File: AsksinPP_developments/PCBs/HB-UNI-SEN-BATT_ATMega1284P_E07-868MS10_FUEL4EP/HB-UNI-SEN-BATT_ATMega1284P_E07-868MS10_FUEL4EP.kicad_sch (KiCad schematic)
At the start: 57 parts, among them J1 Conn_01x02, J10 charge, J11 ePaper connector, J12 FTDI Debuger, J2 Conn_01x02, J3 Conn_01x02, J4 Conn_01x02, J5 ISP Programmer, J6 Conn_01x04, J7 Conn_01x04, J8 Conn_01x04, J9 Conn_01x04, Q1 IRLU024N, SW1 Config button, SW2 Reset button, U1 ATmega1284P-AU, U2 TPS61221DCK, Y1 8MHz

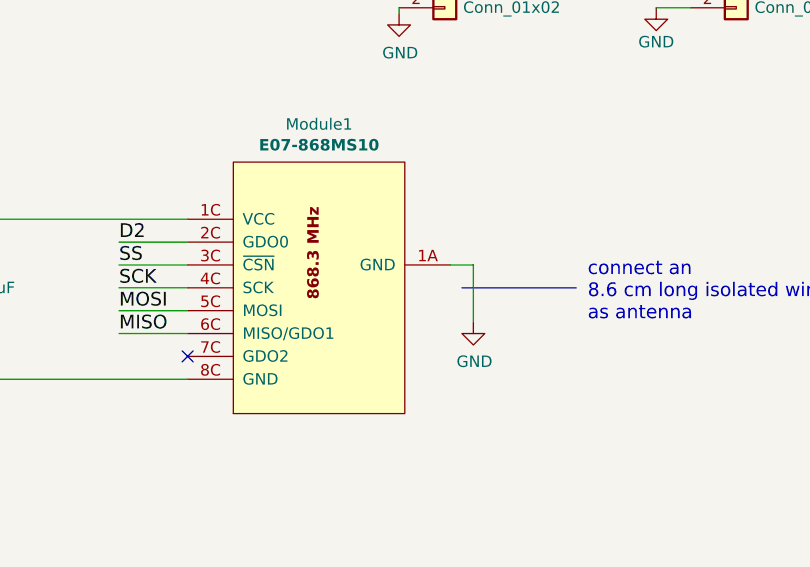
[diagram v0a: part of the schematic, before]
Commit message: PCBs: KiCAD6 required improvements of layout data bases; added E07-900M10S into FUEL and footprint library
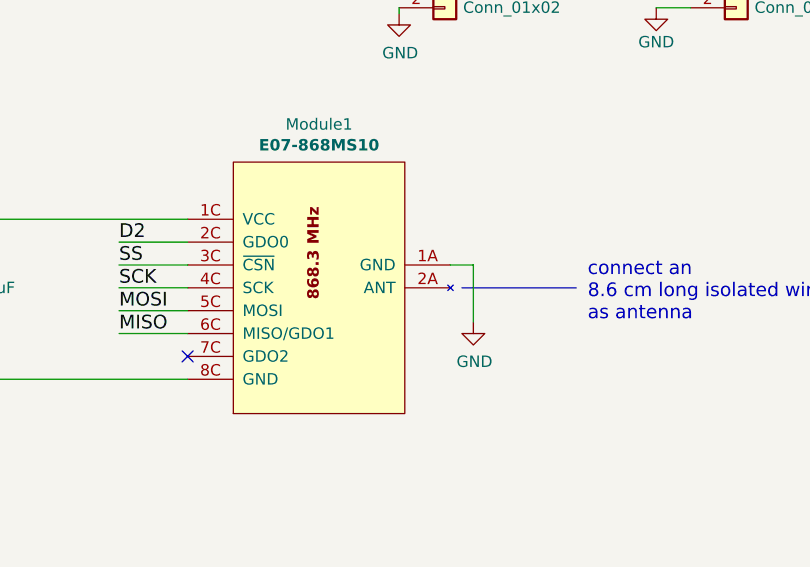
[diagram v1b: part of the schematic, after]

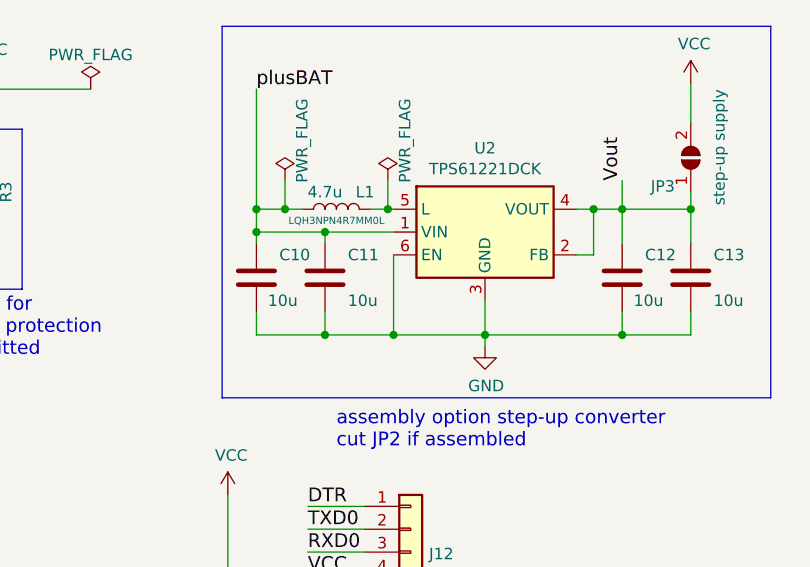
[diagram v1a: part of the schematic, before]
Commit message: HB-UNI-SEN-BATT_ATMega1284P_E07-868MS10_FUEL4EP and HB-UNI-SEN-BATT_ATMega1284P_E07-868MS10_FRAM_FUEL4EP: Fix of wrong connection of EN pin of TPS61221 boost converter
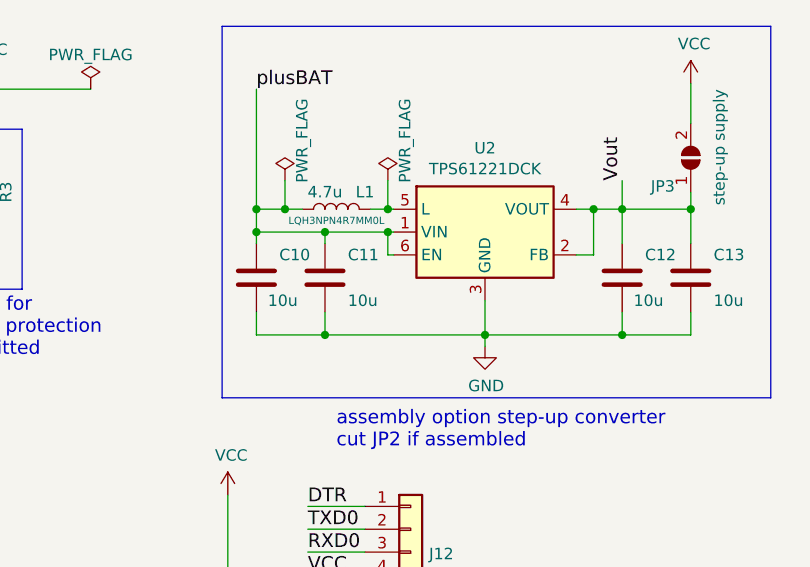
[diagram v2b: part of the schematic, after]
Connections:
- net GND: no longer U2.6 (EN)
- net plusBAT: now also U2.6 (EN)
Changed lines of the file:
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@@
   (title_block
     (title "HB-UNI-SEN-BATT_ATMega1284P_FUEL4EP")
-    (date "2023-07-16")
-    (rev "1.2")
+    (date "2023-08-15")
+    (rev "1.3")
     (company "FUEL4EP")
     (comment 1 "Creative Commons License, non-commercial")
@@
   (junction (at 55.245 28.575) (diameter 0) (color 0 0 0 0)
   )
-  (junction (at 142.24 49.53) (diameter 0) (color 0 0 0 0)
+  (junction (at 141.605 38.1) (diameter 0) (color 0 0 0 0)
   )
   (junction (at 238.76 35.56) (diameter 0) (color 0 0 0 0)
@@
     (stroke (width 0) (type default) (color 0 0 0 0))
   )
-  (wire (pts (xy 134.62 49.53) (xy 142.24 49.53))
+  (wire (pts (xy 134.62 49.53) (xy 152.4 49.53))
     (stroke (width 0) (type default) (color 0 0 0 0))
   )
@@
     (stroke (width 0) (type default) (color 0 0 0 0))
   )
+  (wire (pts (xy 141.605 38.1) (xy 134.62 38.1))
+    (stroke (width 0) (type default) (color 0 0 0 0))
+  )
   (wire (pts (xy 152.4 49.53) (xy 167.64 49.53))
     (stroke (width 0) (type default) (color 0 0 0 0))
@@
     (stroke (width 0) (type default) (color 0 0 0 0))
   )
+  (wire (pts (xy 142.24 40.64) (xy 141.605 40.64))
+    (stroke (width 0) (type default) (color 0 0 0 0))
+  )
   (wire (pts (xy 85.09 110.49) (xy 91.44 110.49))
     (stroke (width 0) (type default) (color 0 0 0 0))
@@
     (stroke (width 0) (type default) (color 0 0 0 0))
   )
+  (wire (pts (xy 141.605 40.64) (xy 141.605 38.1))
+    (stroke (width 0) (type default) (color 0 0 0 0))
+  )
   (wire (pts (xy 201.295 70.485) (xy 202.565 70.485))
     (stroke (width 0) (type default) (color 0 0 0 0))
@@
     (stroke (width 0) (type default) (color 0 0 0 0))
   )
-  (wire (pts (xy 142.24 49.53) (xy 152.4 49.53))
-    (stroke (width 0) (type default) (color 0 0 0 0))
-  )
   (wire (pts (xy 123.825 78.74) (xy 139.065 78.74))
     (stroke (width 0) (type default) (color 0 0 0 0))
@@
     (stroke (width 0) (type default) (color 0 0 0 0))
   )
-  (wire (pts (xy 142.24 40.64) (xy 142.24 49.53))
-    (stroke (width 0) (type default) (color 0 0 0 0))
-  )
   (wire (pts (xy 177.8 116.84) (xy 177.8 116.205))
     (stroke (width 0) (type default) (color 0 0 0 0))
@@
     (stroke (width 0) (type default) (color 0 0 0 0))
   )
-  (wire (pts (xy 142.24 38.1) (xy 134.62 38.1))
-    (stroke (width 0) (type default) (color 0 0 0 0))
-  )
+  (wire (pts (xy 142.24 38.1) (xy 141.605 38.1))
+    (stroke (width 0) (type default) (color 0 0 0 0))
+  )

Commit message: PCBs: added HB-UNI-SEN-BATT_ATMega1284P_E07-900MM10S_FUEL4EP; fies fixes for HB-UNI-SEN-BATT_ATMega1284P_E07-868MS10_FUEL4EP and HB-UNI-SEN-BATT_E07-900MM10S_FUEL4EP
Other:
- title: HB-UNI-SEN-BATT_ATMega1284P_FUEL4EP -> HB-UNI-SEN-BATT_ATMega1284P_E07-868MS10_FUEL4EP
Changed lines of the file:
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@@
   (paper "A4")
   (title_block
-    (title "HB-UNI-SEN-BATT_ATMega1284P_FUEL4EP")
+    (title "HB-UNI-SEN-BATT_ATMega1284P_E07-868MS10_FUEL4EP")
     (date "2023-08-15")
     (rev "1.3")

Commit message: PCBs: documentation updates / PCBs: HB-UNI-SEN-BATT_ATMega1284P_E07-868MS10_FUEL4EP, HB-UNI-SEN-BATT_ATMega1284P_E07-868MS10_FRAM_FUEL4EP, HB-UNI-SEN-BATT_ATMega1284P_E07-900MM10S_FUEL4EP: fix of wrong LCSC number for R7
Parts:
- R7: LCSC C25271 -> C149504
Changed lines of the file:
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@@
   (title_block
     (title "HB-UNI-SEN-BATT_ATMega1284P_E07-868MS10_FUEL4EP")
-    (date "2023-08-15")
-    (rev "1.3")
+    (date "2024-02-17")
+    (rev "1.4")
     (company "FUEL4EP")
     (comment 1 "Creative Commons License, non-commercial")
@@
       (effects (font (size 1.27 1.27)) hide)
     )
-    (property "Datasheet" "https://datasheet.lcsc.com/lcsc/1809140123_UNI-ROYAL-Uniroyal-Elec-0805W8F100KT5E_C25271.pdf" (id 3) (at 197.485 70.485 0)
+    (property "Datasheet" "https://datasheet.lcsc.com/lcsc/2205312316_UNI-ROYAL-Uniroyal-Elec-0805W8F1003T5E_C149504.pdf" (id 3) (at 197.485 70.485 0)
       (effects (font (size 1.27 1.27)) hide)
     )
@@
       (effects (font (size 1.27 1.27)) hide)
     )
-    (property "LCSC" "C25271" (id 5) (at 197.485 70.485 0)
-      (effects (font (size 1.27 1.27)) hide)
-    )
+    (property "LCSC" "C149504" (id 5) (at 197.485 70.485 0)
+      (effects (font (size 1.27 1.27)) hide)
+    )

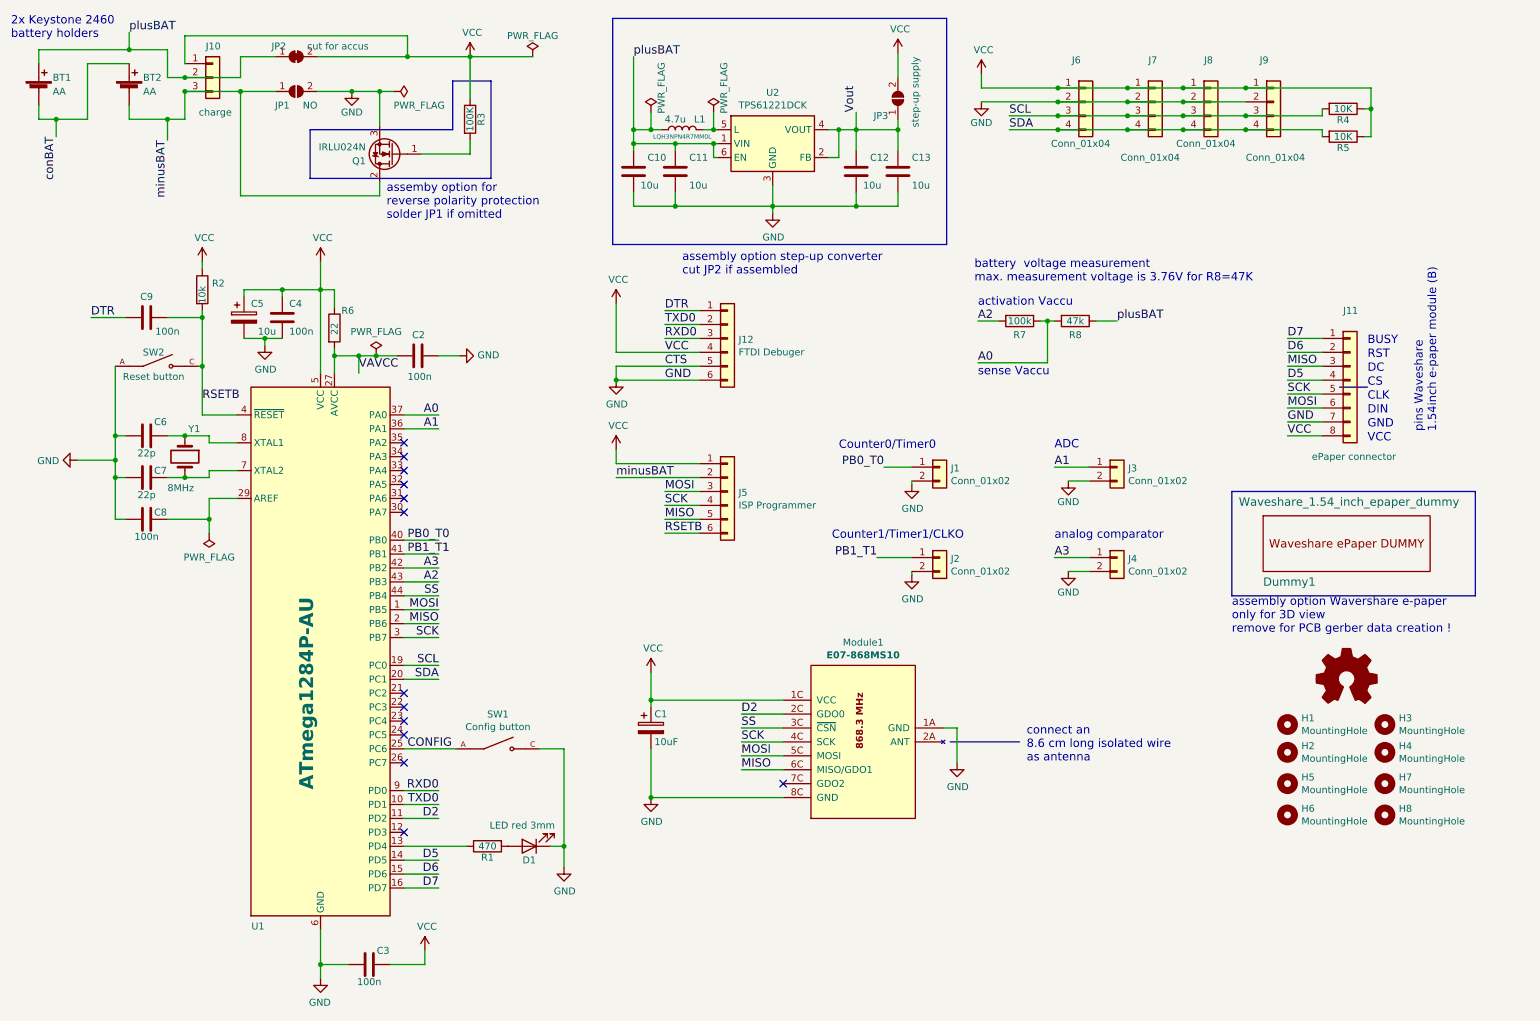
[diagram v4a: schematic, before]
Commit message: PCBs/HB-UNI-SEN-BATT_ATMega1284P_E07-868MS10_FUEL4EP: migration to KiCAD 8, x-check and fix of LCSC numbers
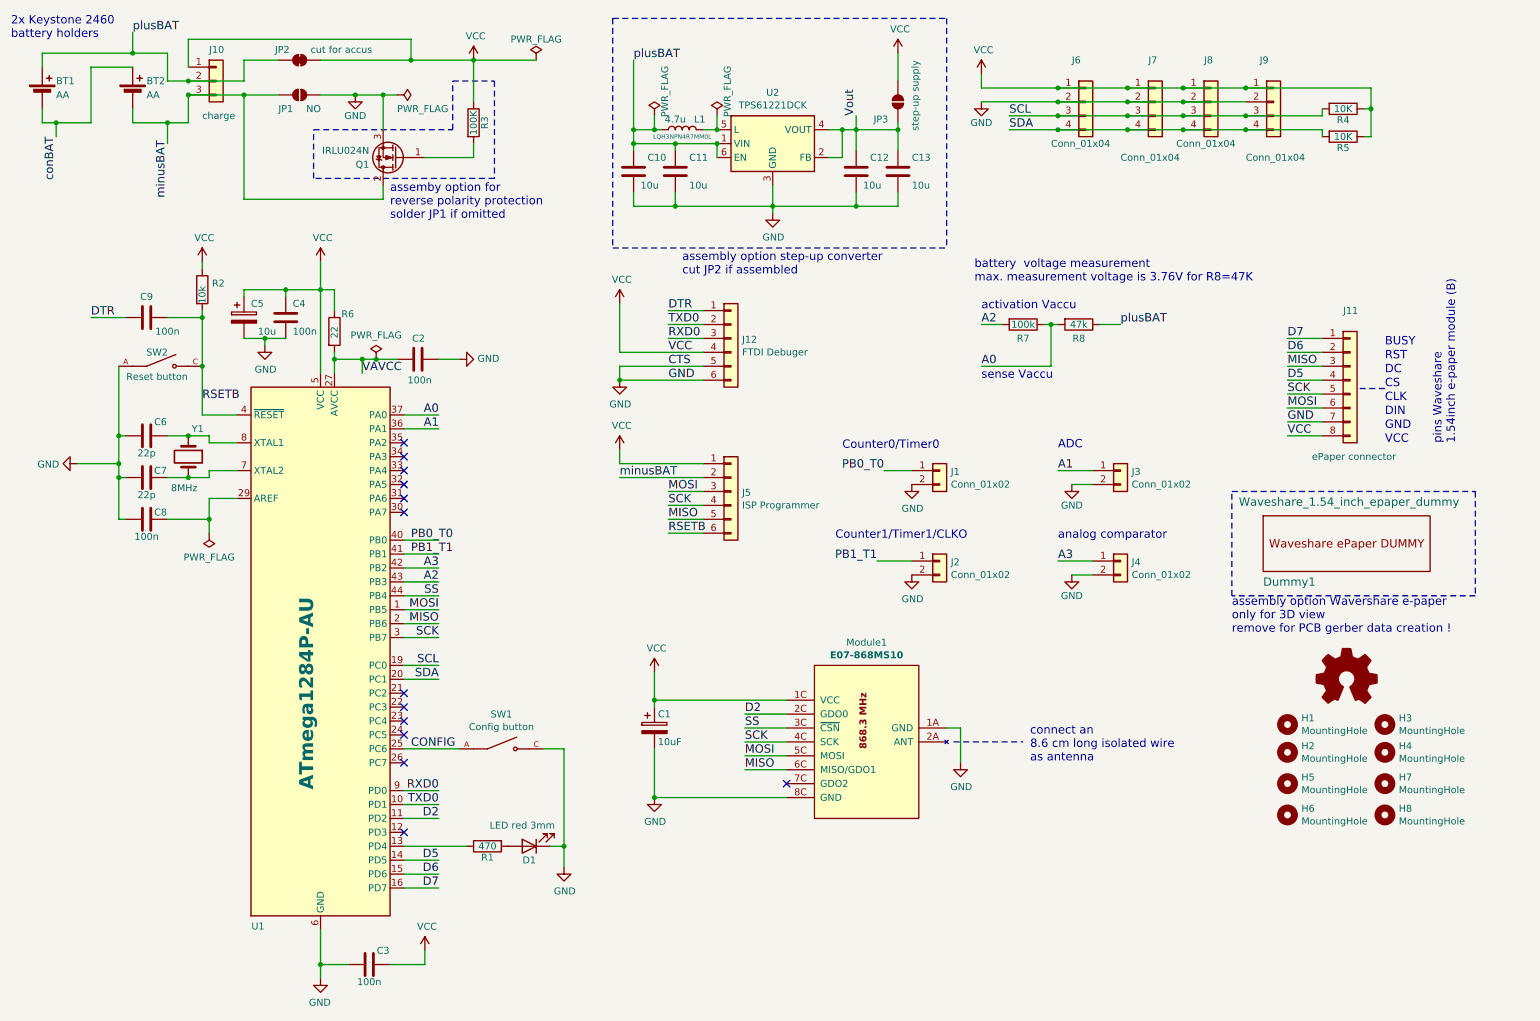
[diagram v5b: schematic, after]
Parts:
- R2: LCSC C17733 -> C17414
- R4, R5: LCSC C101933 -> C17414; TYPE R0805 -> 0805
- U1: TYPE TQFP-44_10.0x10.0x0.8P -> TQFP-44(10x10)
- U2: LCSC C37055 -> C2865756; TYPE SOT-363 -> SC-70-6
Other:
- moved on the sheet: BT1, BT2, C1, C2, C4, J1, J10, J12, J2, J3, J4, J5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
